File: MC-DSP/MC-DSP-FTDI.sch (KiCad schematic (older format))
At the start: 46 parts, among them U200 FT2232HL, U201 TPD2S017, U202 USB_B, U203 AZ1117-3.3, U204 ISO7730DW, U205 ISO7730DW, U206 ISO7730DW, U207 Crystal_GND24

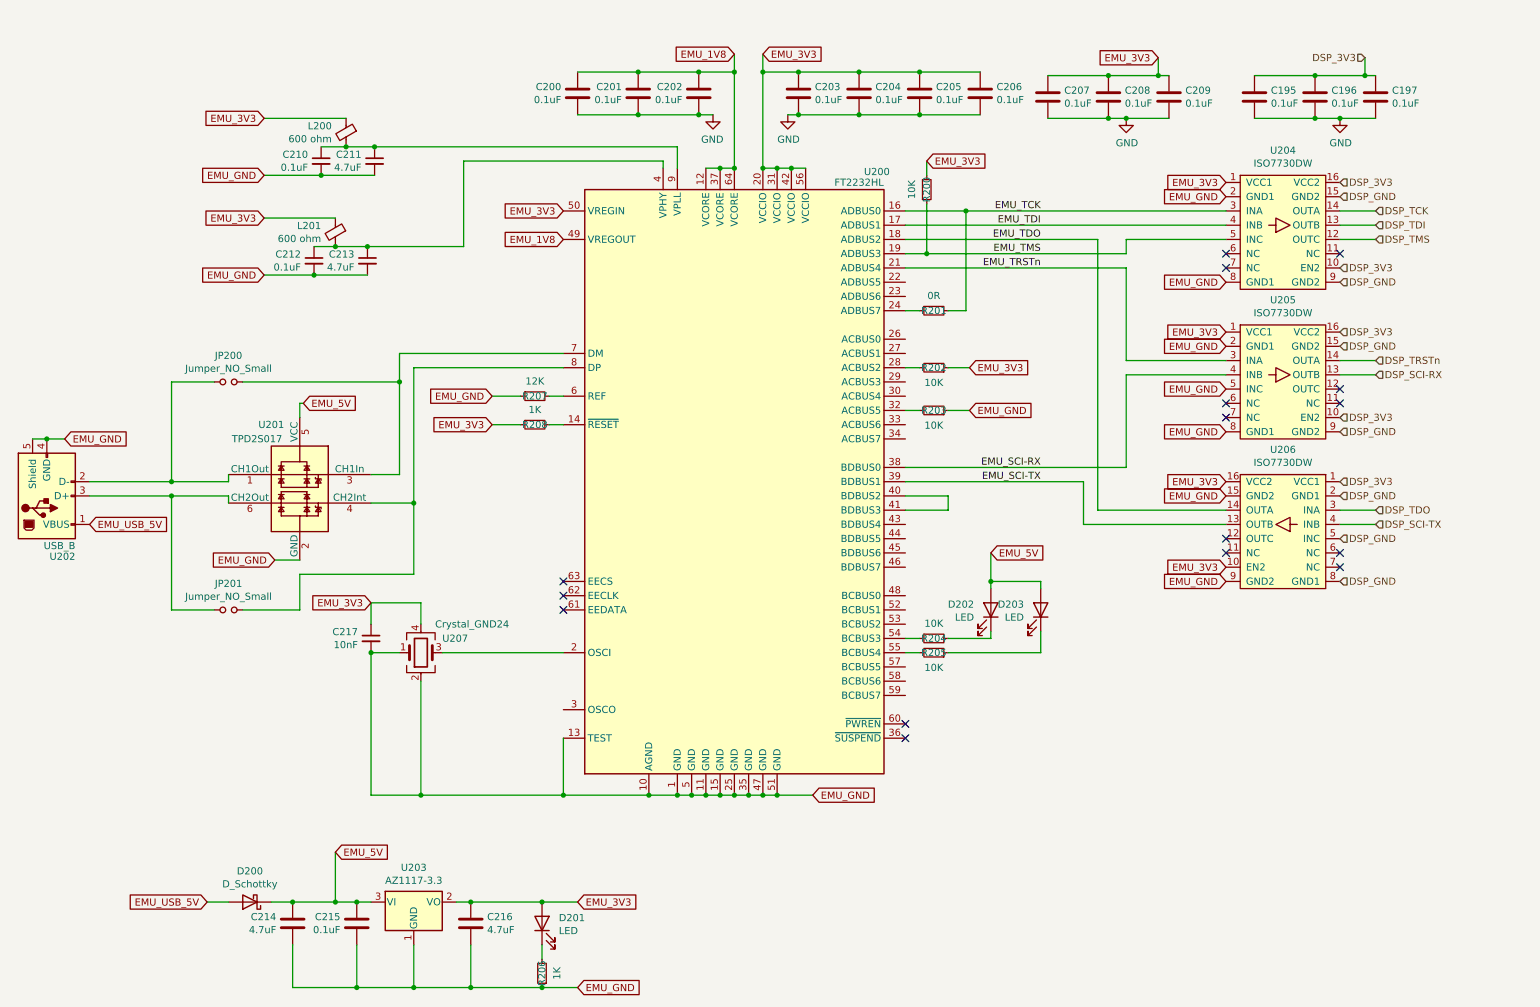
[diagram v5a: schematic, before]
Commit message: added backplane connector, changed right angle headers, added FP for bigger reg caps, all ICs arranged, routed isolated section.
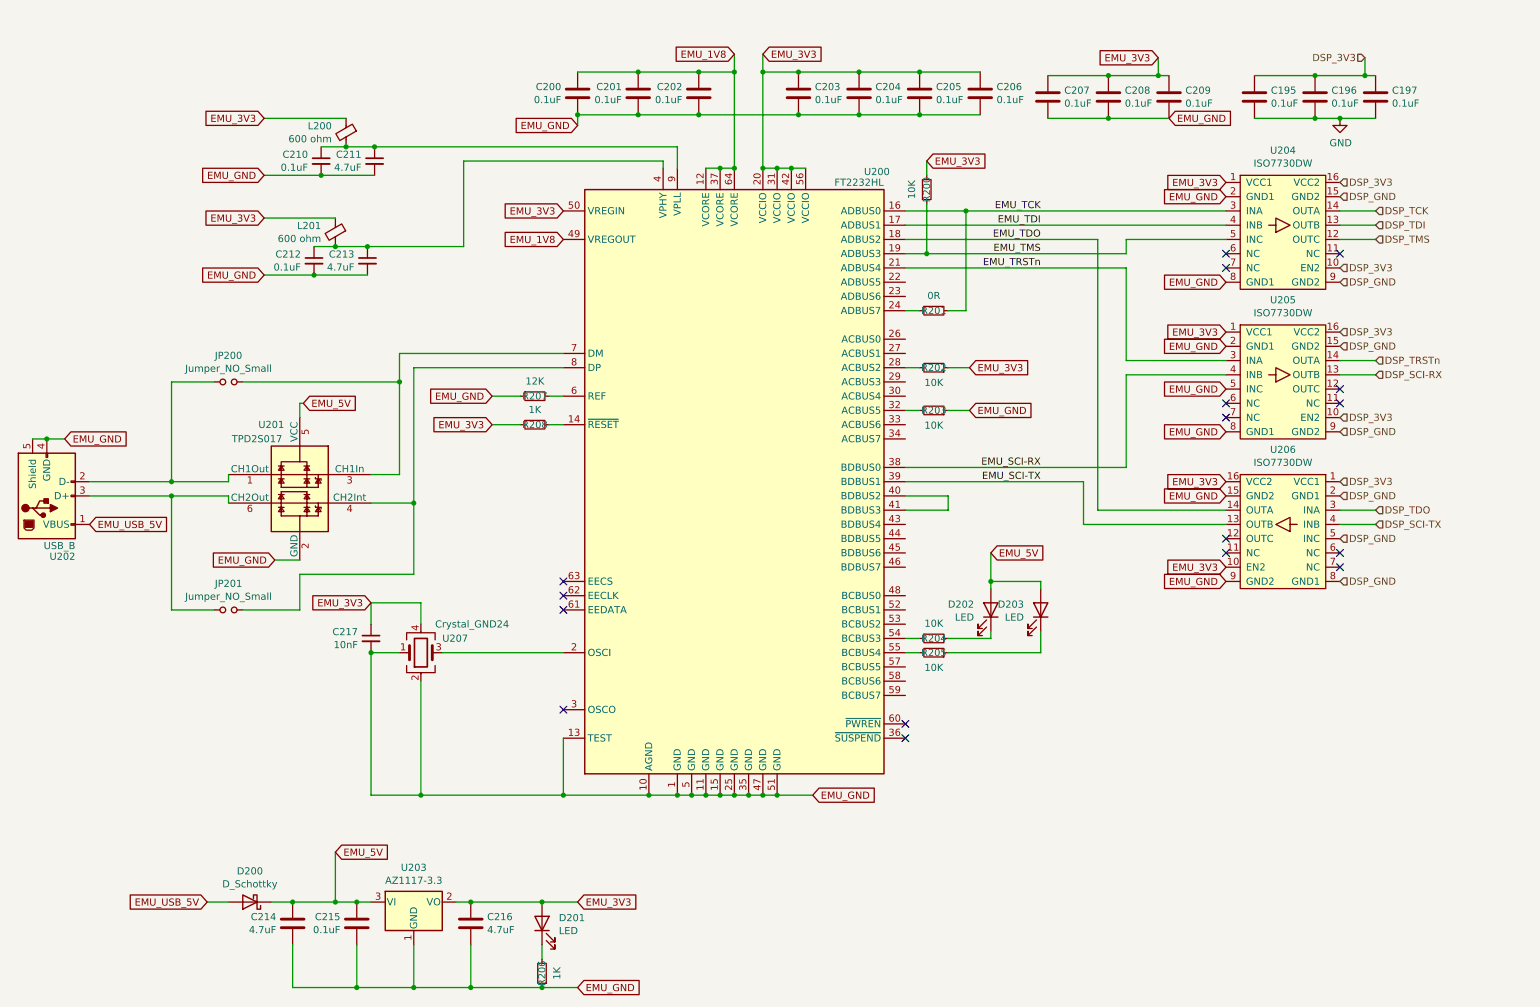
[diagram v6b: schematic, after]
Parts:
- U207: footprint ???????? -> Oscillator:Oscillator_SMD_TXC_7C-4Pin_5.0x3.2mm_HandSoldering
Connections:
- net EMU_GND: now also C200.2, C201.2, C202.2, C203.2, C204.2, C205.2, C206.2, C207.2, C208.2, C209.2
- net GND: no longer C200.2, C201.2, C202.2, C203.2, C204.2, C205.2, C206.2, C207.2, C208.2, C209.2
- no-connect marks 16 -> 17
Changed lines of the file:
@@
 $Descr A4 11693 8268
 encoding utf-8
-Sheet 7 7
+Sheet 5 6
 Title ""
 Date ""
@@
 Wire Wire Line
 	5700 925  5700 800
-$Comp
-L power:GND #PWR0182
-U 1 1 6197FA90
-P 5550 1225
-F 0 "#PWR0182" H 5550 975 50  0001 C CNN
-F 1 "GND" H 5555 1052 50  0000 C CNN
-F 2 "" H 5550 1225 50  0001 C CNN
-F 3 "" H 5550 1225 50  0001 C CNN
-	1    5550 1225
-	-1   0    0    -1
-$EndComp
 Wire Wire Line
 	5700 925  5450 925
@@
 Wire Wire Line
 	5900 800  5900 925
-$Comp
-L power:GND #PWR0183
-U 1 1 61999F10
-P 6075 1225
-F 0 "#PWR0183" H 6075 975 50  0001 C CNN
-F 1 "GND" H 6080 1052 50  0000 C CNN
-F 2 "" H 6075 1225 50  0001 C CNN
-F 3 "" H 6075 1225 50  0001 C CNN
-	1    6075 1225
-	1    0    0    -1
-$EndComp
 Wire Wire Line
 	5900 925  6150 925
@@
 Wire Wire Line
 	6150 925  6575 925
-Wire Wire Line
-	6150 1225 6575 1225
 $Comp
 L Device:C C204
@@
 	2150 3900 2150 3950
 Connection ~ 6150 1225
-Wire Wire Line
-	6150 1225 6075 1225
 Connection ~ 5450 1225
-Wire Wire Line
-	5450 1225 5550 1225
 $Comp
 L Device:R_Small R207
@@
 F 0 "U207" H 3650 4900 50  0000 L CNN
 F 1 "Crystal_GND24" H 3600 4800 50  0000 L CNN
-F 2 "????????" H 3500 5000 50  0001 C CNN
+F 2 "Oscillator:Oscillator_SMD_TXC_7C-4Pin_5.0x3.2mm_HandSoldering" H 3500 5000 50  0001 C CNN
 F 3 "https://www.digikey.com/en/products/detail/abracon-llc/ASFL1-12-000MHZ-L-T/2623936" H 3500 5000 50  0001 C CNN
 	1    3500 5000
@@
 Wire Wire Line
 	7200 2600 7325 2600
-Wire Wire Line
-	7325 2600 7325 1900
 Connection ~ 7325 1900
 Connection ~ 7050 2200
@@
 	5200 1600 5200 1550
 Wire Wire Line
-	5200 1550 3800 1550
-Wire Wire Line
 	7000 5000 6900 5000
 Wire Wire Line
@@
 Wire Wire Line
 	7050 1650 7050 1550
-Text GLabel 2400 1250 0    50   Input ~ 0
-EMU_3V3
 Text GLabel 5700 800  0    50   Input ~ 0
 EMU_1V8
@@
 Wire Wire Line
 	4500 6000 5100 6000
-$Comp
-L Interface_USB:FT2232HL U200
-U 1 1 61F8D5E7
-P 5700 3800
-F 0 "U200" H 6700 5975 50  0000 C CNN
-F 1 "FT2232HL" H 6575 5900 50  0000 C CNN
-F 2 "Package_QFP:LQFP-64_10x10mm_P0.5mm" H 5700 3800 50  0001 C CNN
-F 3 "~" H 5700 3800 50  0001 C CNN
-	1    5700 3800
-	1    0    0    -1
-$EndComp
 Text GLabel 4000 3200 0    50   Input ~ 0
 EMU_GND
@@
 	1    0    0    -1
 $EndComp
-$Comp
-L Device:LED D201
-U 1 1 62148017
-P 4350 6900
-F 0 "D201" V 4389 6782 50  0000 R CNN
-F 1 "LED" V 4298 6782 50  0000 R CNN
-F 2 "LED_THT:LED_D3.0mm" H 4350 6900 50  0001 C CNN
-F 3 "~" H 4350 6900 50  0001 C CNN
-	1    4350 6900
-	0    -1   -1   0
-$EndComp
-$Comp
-L Device:R_Small R206
-U 1 1 62148CAF
-P 4350 7250
-F 0 "R206" V 4350 7250 50  0000 C CNN
-F 1 "1K" V 4245 7250 50  0000 C CNN
-F 2 "Resistor_SMD:R_0603_1608Metric_Pad0.98x0.95mm_HandSolder" H 4350 7250 50  0001 C CNN
-F 3 "https://www.digikey.com/en/products/detail/yageo/RC0603FR-071KL/726843" H 4350 7250 50  0001 C CNN
-	1    4350 7250
-	-1   0    0    1
-$EndComp
 Wire Wire Line
 	3450 7350 3450 7050
@@
 Wire Wire Line
 	3850 7350 3450 7350
-Wire Wire Line
-	4350 7150 4350 7050
-Wire Wire Line
-	3850 6750 4350 6750
-Wire Wire Line
-	3850 7350 4350 7350
-Connection ~ 4350 6750
-Wire Wire Line
-	4350 6750 4600 6750
-Connection ~ 4350 7350
-Wire Wire Line
-	4350 7350 4600 7350
 $Comp
 L Device:C C215
@@
 F 1 "TPD2S017" H 2950 4200 50  0000 C CNN
 F 2 "Package_TO_SOT_SMD:SOT-23-6" H 1900 3500 50  0001 C CNN
-F 3 "????" H 2650 3850 50  0001 C CNN
+F 3 "????????" H 2650 3850 50  0001 C CNN
 	1    2650 3850
 	-1   0    0    -1
@@
 	8675 825  8675 950
 $Comp
-L power:GND #PWR0184
-U 1 1 62507ACB
-P 8450 1250
-F 0 "#PWR0184" H 8450 1000 50  0001 C CNN
-F 1 "GND" H 8455 1077 50  0000 C CNN
-F 2 "" H 8450 1250 50  0001 C CNN
-F 3 "" H 8450 1250 50  0001 C CNN
-	1    8450 1250
-	1    0    0    -1
-$EndComp
-$Comp
 L Device:C C207
 U 1 1 62507ADB
@@
 Wire Wire Line
 	8675 950  8750 950
-Wire Wire Line
-	8750 1250 8450 1250
 Text HLabel 9950 2300 2    50   Input ~ 0
 DSP_3V3
@@
 Wire Wire Line
 	9950 1250 9775 1250
-Connection ~ 8450 1250
-Wire Wire Line
-	8450 1250 8325 1250
 Wire Wire Line
 	8325 1250 7900 1250
@@
 	3450 4450 3450 3950
 Connection ~ 3450 3950
+NoConn ~ 4500 5400
+Wire Wire Line
+	4350 7150 4350 7050
+Wire Wire Line
+	4350 7350 4600 7350
+Wire Wire Line
+	3850 7350 4350 7350
+Connection ~ 4350 7350
+$Comp
+L Device:R_Small R206
+U 1 1 62148CAF
+P 4350 7250
+F 0 "R206" V 4350 7250 50  0000 C CNN
+F 1 "1K" V 4245 7250 50  0000 C CNN
+F 2 "Resistor_SMD:R_0603_1608Metric_Pad0.98x0.95mm_HandSolder" H 4350 7250 50  0001 C CNN
+F 3 "https://www.digikey.com/en/products/detail/yageo/RC0603FR-071KL/726843" H 4350 7250 50  0001 C CNN
+	1    4350 7250
+	-1   0    0    1
+$EndComp
+Wire Wire Line
+	4350 6750 4600 6750
+Wire Wire Line
+	3850 6750 4350 6750
+Connection ~ 4350 6750
+$Comp
+L Device:LED D201
+U 1 1 62148017
+P 4350 6900
+F 0 "D201" V 4389 6782 50  0000 R CNN
+F 1 "LED" V 4298 6782 50  0000 R CNN
+F 2 "LED_THT:LED_D3.0mm" H 4350 6900 50  0001 C CNN
+F 3 "~" H 4350 6900 50  0001 C CNN
+	1    4350 6900
+	0    -1   -1   0
+$EndComp
+Wire Wire Line
+	5200 1550 3800 1550
+Text GLabel 4600 1300 0    50   Input ~ 0
+EMU_GND
+Wire Wire Line
+	4600 1300 4600 1225
+Connection ~ 4600 1225
+Wire Wire Line
+	6150 1225 6575 1225
+Wire Wire Line
+	5450 1225 6150 1225
+Wire Wire Line
+	8325 1250 8750 1250
+Text GLabel 8750 1250 2    50   Input ~ 0
+EMU_GND
+Wire Wire Line
+	7325 2600 7325 1900
+$Comp
+L Interface_USB:FT2232HL U200
+U 1 1 61F8D5E7
+P 5700 3800
+F 0 "U200" H 6700 5975 50  0000 C CNN
+F 1 "FT2232HL" H 6575 5900 50  0000 C CNN
+F 2 "Package_QFP:LQFP-64_10x10mm_P0.5mm" H 5700 3800 50  0001 C CNN
+F 3 "~" H 5700 3800 50  0001 C CNN
+	1    5700 3800
+	1    0    0    -1
+$EndComp
+Text GLabel 2400 1250 0    50   Input ~ 0
+EMU_3V3
 $EndSCHEMATC

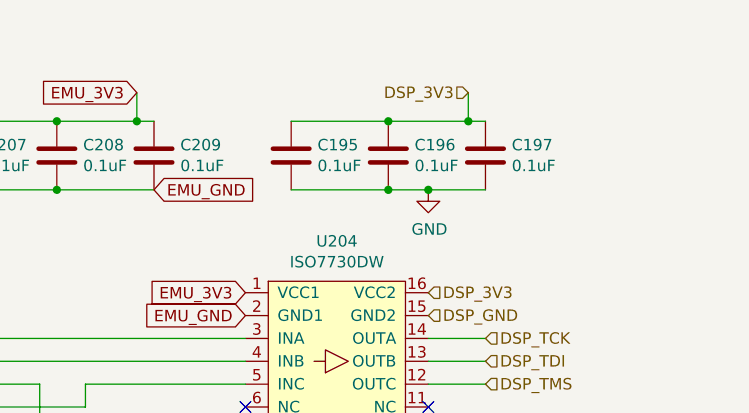
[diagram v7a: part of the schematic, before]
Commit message: Total overhaul of power planes. Routed whole Analog section, middle of digital section.
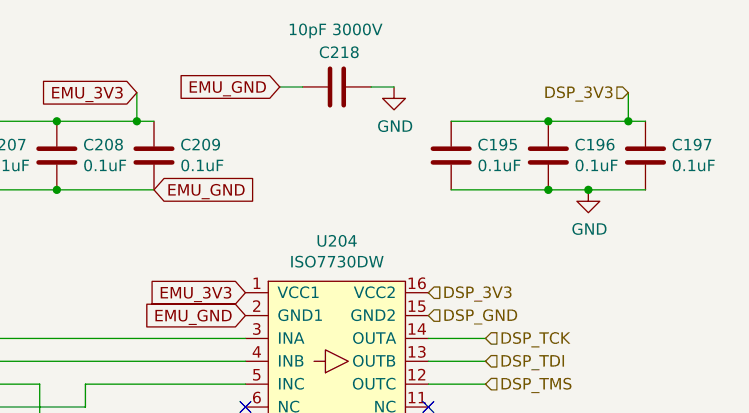
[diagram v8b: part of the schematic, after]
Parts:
- added C218: 10pF 3000V, Capacitor_SMD:C_1812_4532Metric_Pad1.57x3.40mm_HandSolder, symbol Device:C
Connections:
- net EMU_GND: now also C218.1
- net GND: now also C218.2
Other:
- moved on the sheet: C195, C196, C197
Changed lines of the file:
@@
 $Descr A4 11693 8268
 encoding utf-8
-Sheet 5 7
+Sheet 3 7
 Title ""
 Date ""
@@
 $EndComp
 Wire Wire Line
-	10125 825  10125 950
+	10825 825  10825 950
 $Comp
 L Device:C C195
 U 1 1 62548433
-P 9350 1100
-F 0 "C195" H 9465 1146 50  0000 L CNN
-F 1 "0.1uF" H 9465 1055 50  0000 L CNN
-F 2 "Capacitor_SMD:C_0603_1608Metric_Pad1.08x0.95mm_HandSolder" H 9388 950 50  0001 C CNN
-F 3 "https://www.digikey.com/en/products/detail/yageo/CC0603KRX7R9BB104/2103082" H 9350 1100 50  0001 C CNN
-	1    9350 1100
-	1    0    0    -1
-$EndComp
-Wire Wire Line
-	9350 950  9775 950
+P 10050 1100
+F 0 "C195" H 10165 1146 50  0000 L CNN
+F 1 "0.1uF" H 10165 1055 50  0000 L CNN
+F 2 "Capacitor_SMD:C_0603_1608Metric_Pad1.08x0.95mm_HandSolder" H 10088 950 50  0001 C CNN
+F 3 "https://www.digikey.com/en/products/detail/yageo/CC0603KRX7R9BB104/2103082" H 10050 1100 50  0001 C CNN
+	1    10050 1100
+	1    0    0    -1
+$EndComp
+Wire Wire Line
+	10050 950  10475 950
 $Comp
 L Device:C C196
 U 1 1 6254843B
-P 9775 1100
-F 0 "C196" H 9890 1146 50  0000 L CNN
-F 1 "0.1uF" H 9890 1055 50  0000 L CNN
-F 2 "Capacitor_SMD:C_0603_1608Metric_Pad1.08x0.95mm_HandSolder" H 9813 950 50  0001 C CNN
-F 3 "https://www.digikey.com/en/products/detail/yageo/CC0603KRX7R9BB104/2103082" H 9775 1100 50  0001 C CNN
-	1    9775 1100
-	1    0    0    -1
-$EndComp
-Connection ~ 9775 950
-Connection ~ 9775 1250
+P 10475 1100
+F 0 "C196" H 10590 1146 50  0000 L CNN
+F 1 "0.1uF" H 10590 1055 50  0000 L CNN
+F 2 "Capacitor_SMD:C_0603_1608Metric_Pad1.08x0.95mm_HandSolder" H 10513 950 50  0001 C CNN
+F 3 "https://www.digikey.com/en/products/detail/yageo/CC0603KRX7R9BB104/2103082" H 10475 1100 50  0001 C CNN
+	1    10475 1100
+	1    0    0    -1
+$EndComp
+Connection ~ 10475 950
+Connection ~ 10475 1250
 $Comp
 L Device:C C197
 U 1 1 62548443
-P 10200 1100
-F 0 "C197" H 10315 1146 50  0000 L CNN
-F 1 "0.1uF" H 10315 1055 50  0000 L CNN
-F 2 "Capacitor_SMD:C_0603_1608Metric_Pad1.08x0.95mm_HandSolder" H 10238 950 50  0001 C CNN
-F 3 "https://www.digikey.com/en/products/detail/yageo/CC0603KRX7R9BB104/2103082" H 10200 1100 50  0001 C CNN
-	1    10200 1100
-	1    0    0    -1
-$EndComp
-Wire Wire Line
-	9775 950  10125 950
-Connection ~ 10125 950
-Wire Wire Line
-	10125 950  10200 950
-Wire Wire Line
-	10200 1250 9950 1250
-Text HLabel 10125 825  0    50   Input ~ 0
+P 10900 1100
+F 0 "C197" H 11015 1146 50  0000 L CNN
+F 1 "0.1uF" H 11015 1055 50  0000 L CNN
+F 2 "Capacitor_SMD:C_0603_1608Metric_Pad1.08x0.95mm_HandSolder" H 10938 950 50  0001 C CNN
+F 3 "https://www.digikey.com/en/products/detail/yageo/CC0603KRX7R9BB104/2103082" H 10900 1100 50  0001 C CNN
+	1    10900 1100
+	1    0    0    -1
+$EndComp
+Wire Wire Line
+	10475 950  10825 950
+Connection ~ 10825 950
+Wire Wire Line
+	10825 950  10900 950
+Wire Wire Line
+	10900 1250 10650 1250
+Text HLabel 10825 825  0    50   Input ~ 0
 DSP_3V3
 $Comp
 L power:GND #PWR0185
 U 1 1 6254842D
-P 9950 1250
-F 0 "#PWR0185" H 9950 1000 50  0001 C CNN
-F 1 "GND" H 9955 1077 50  0000 C CNN
-F 2 "" H 9950 1250 50  0001 C CNN
-F 3 "" H 9950 1250 50  0001 C CNN
-	1    9950 1250
-	1    0    0    -1
-$EndComp
-Connection ~ 9950 1250
-Wire Wire Line
-	9950 1250 9775 1250
+P 10650 1250
+F 0 "#PWR0185" H 10650 1000 50  0001 C CNN
+F 1 "GND" H 10655 1077 50  0000 C CNN
+F 2 "" H 10650 1250 50  0001 C CNN
+F 3 "" H 10650 1250 50  0001 C CNN
+	1    10650 1250
+	1    0    0    -1
+$EndComp
+Connection ~ 10650 1250
+Wire Wire Line
+	10650 1250 10475 1250
 Wire Wire Line
 	8325 1250 7900 1250
 Wire Wire Line
-	9775 1250 9350 1250
+	10475 1250 10050 1250
 $Comp
 L Device:C_Small C217
@@
 Text GLabel 2400 1250 0    50   Input ~ 0
 EMU_3V3
+$Comp
+L Device:C C218
+U 1 1 625764BD
+P 9550 800
+F 0 "C218" V 9700 700 50  0000 L CNN
+F 1 "10pF 3000V" V 9800 600 50  0000 L CNN
+F 2 "Capacitor_SMD:C_1812_4532Metric_Pad1.57x3.40mm_HandSolder" H 9588 650 50  0001 C CNN
+F 3 "https://www.digikey.com/en/products/detail/yageo/CC1812JKNPOEBN100/5884813" H 9550 800 50  0001 C CNN
+	1    9550 800
+	0    -1   -1   0
+$EndComp
+Text GLabel 9300 800  0    50   Input ~ 0
+EMU_GND
+$Comp
+L power:GND #PWR0132
+U 1 1 62578C81
+P 9800 800
+F 0 "#PWR0132" H 9800 550 50  0001 C CNN
+F 1 "GND" H 9805 627 50  0000 C CNN
+F 2 "" H 9800 800 50  0001 C CNN
+F 3 "" H 9800 800 50  0001 C CNN
+	1    9800 800
+	1    0    0    -1
+$EndComp
+Wire Wire Line
+	9300 800  9400 800
+Wire Wire Line
+	9700 800  9800 800
 $EndSCHEMATC
